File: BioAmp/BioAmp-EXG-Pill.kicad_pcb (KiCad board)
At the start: 2 copper layers, 39.2 x 11 mm, 21 parts, among them IC1 MCP3221A4T-E_OT, J1 Conn_01x03_Pin, J2 Conn_01x04_Pin, J3 Conn_01x04_Pin, U1 Amp

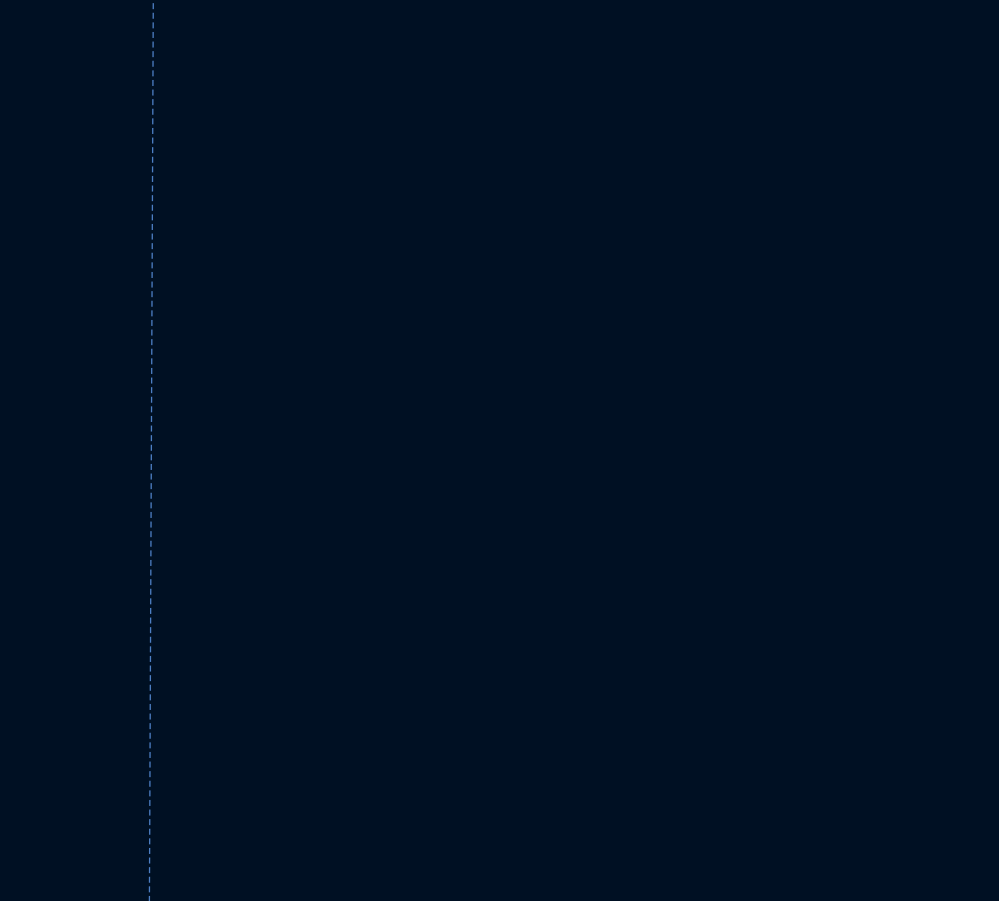
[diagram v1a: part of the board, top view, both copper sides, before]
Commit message: Added new ADC and cleaned up ESD protection
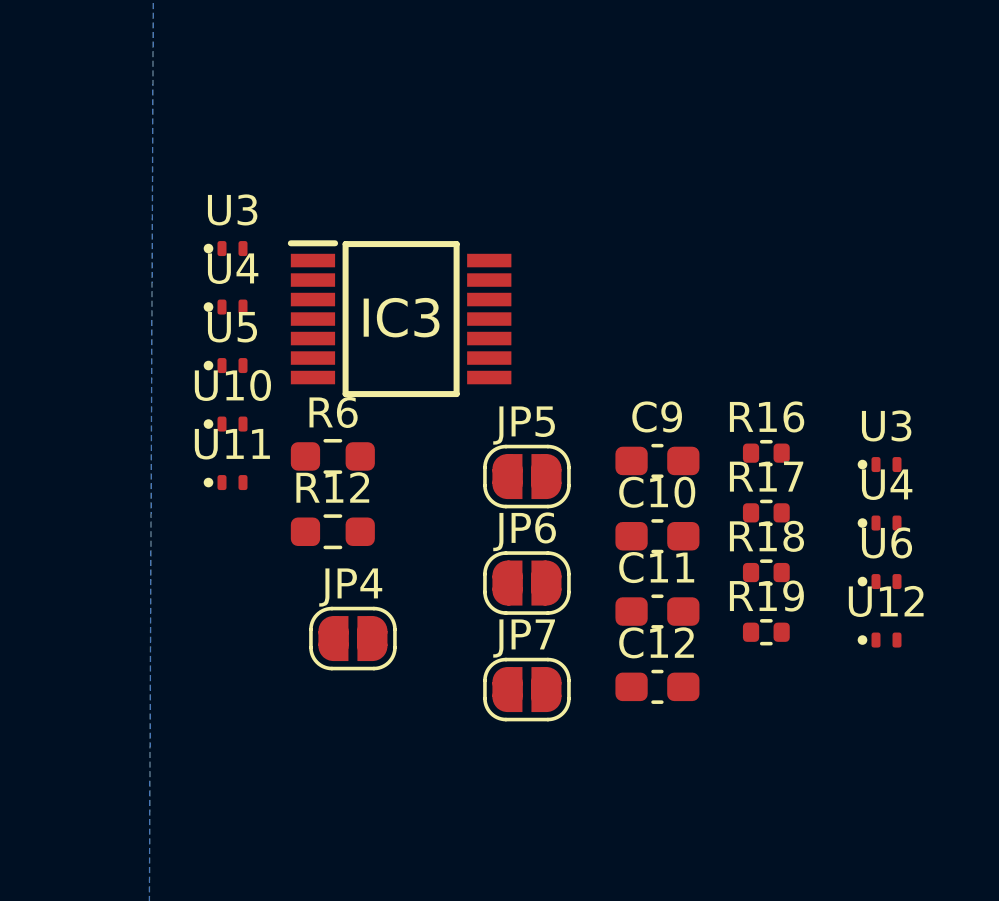
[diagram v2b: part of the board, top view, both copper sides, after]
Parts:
- added C10: 100n, Capacitor_SMD:C_0603_1608Metric_Pad1.08x0.95mm_HandSolder, F.Cu at (176.8, 99.1)
- added C11: 100n, Capacitor_SMD:C_0603_1608Metric_Pad1.08x0.95mm_HandSolder, F.Cu at (176.8, 101.6)
- added C12: 100n, Capacitor_SMD:C_0603_1608Metric_Pad1.08x0.95mm_HandSolder, F.Cu at (176.8, 104.1)
- added C9: 100n, Capacitor_SMD:C_0603_1608Metric_Pad1.08x0.95mm_HandSolder, F.Cu at (176.8, 96.6)
- added IC3: MAX1169BEUD+, MAX1169:SOP65P640X110-14N, F.Cu at (168.3, 91.8)
- added JP4: SolderJumper_2_Open, Jumper:SolderJumper-2_P1.3mm_Open_RoundedPad1.0x1.5mm, F.Cu at (166.7, 102.5)
- added JP5: SolderJumper_2_Open, Jumper:SolderJumper-2_P1.3mm_Open_RoundedPad1.0x1.5mm, F.Cu at (172.5, 97.1)
- added JP6: SolderJumper_2_Open, Jumper:SolderJumper-2_P1.3mm_Open_RoundedPad1.0x1.5mm, F.Cu at (172.5, 100.6)
- added JP7: SolderJumper_2_Open, Jumper:SolderJumper-2_P1.3mm_Open_RoundedPad1.0x1.5mm, F.Cu at (172.5, 104.2)
- added R12: 2.2K, Resistor_SMD:R_0603_1608Metric_Pad0.98x0.95mm_HandSolder, F.Cu at (166.0, 98.9)
- added R16: 10k, Resistor_SMD:R_0402_1005Metric, F.Cu at (180.5, 96.3)
- added R17: 10k, Resistor_SMD:R_0402_1005Metric, F.Cu at (180.5, 98.3)
- added R18: 10k, Resistor_SMD:R_0402_1005Metric, F.Cu at (180.5, 100.3)
- added R19: 10k, Resistor_SMD:R_0402_1005Metric, F.Cu at (180.5, 102.3)
- added R6: 2.2K, Resistor_SMD:R_0603_1608Metric_Pad0.98x0.95mm_HandSolder, F.Cu at (166.0, 96.4)
- added U10: TPD1E05U06DPY, Package_SON:Texas_DPY0002A_0.6x1mm_P0.65mm, F.Cu at (162.7, 95.3)
- added U11: TPD1E05U06DPY, Package_SON:Texas_DPY0002A_0.6x1mm_P0.65mm, F.Cu at (162.7, 97.3)
- added U12: TPD1E05U06DPY, Package_SON:Texas_DPY0002A_0.6x1mm_P0.65mm, F.Cu at (184.5, 102.5)
- added U3: TPD1E05U06DPY, Package_SON:Texas_DPY0002A_0.6x1mm_P0.65mm, F.Cu at (162.7, 89.5)
- added U3: TPD1E05U06DPY, Package_SON:Texas_DPY0002A_0.6x1mm_P0.65mm, F.Cu at (184.5, 96.7)
- added U4: TPD1E05U06DPY, Package_SON:Texas_DPY0002A_0.6x1mm_P0.65mm, F.Cu at (184.5, 98.6)
- added U4: TPD1E05U06DPY, Package_SON:Texas_DPY0002A_0.6x1mm_P0.65mm, F.Cu at (162.7, 91.4)
- added U5: TPD1E05U06DPY, Package_SON:Texas_DPY0002A_0.6x1mm_P0.65mm, F.Cu at (162.7, 93.4)
- added U6: TPD1E05U06DPY, Package_SON:Texas_DPY0002A_0.6x1mm_P0.65mm, F.Cu at (184.5, 100.6)
- C1: value 47uF -> 8.2uF
- C2: value 1nF -> 4.3nF
- C4: value 1nF -> 10pF
- R11: value 0R -> 1M
- R3: value 1M -> 100k
- R4: value 220K -> 270k
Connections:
- IC1 pad 4: SDA -> Net-(IC1-SDA)
- U1 pad 3: IN- -> Net-(U1A-+)
- U1 pad 5: IN+ -> Net-(U1B-+)

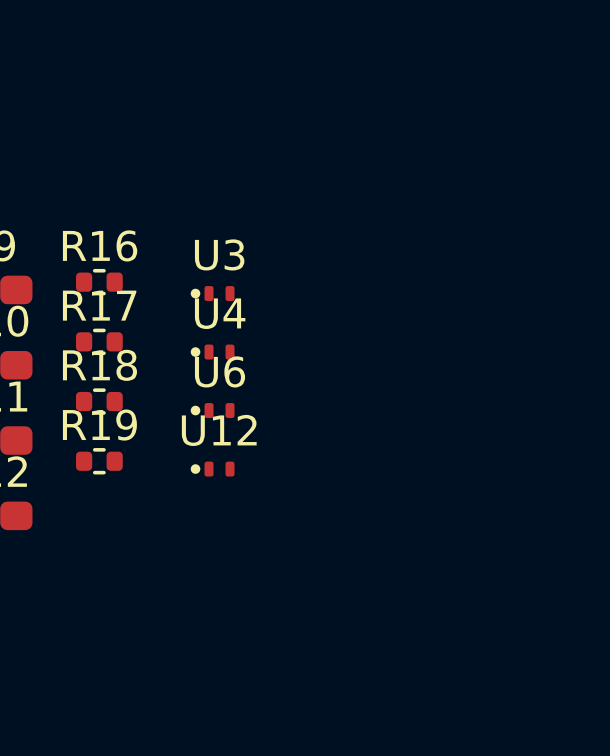
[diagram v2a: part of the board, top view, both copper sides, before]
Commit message: Added series resitors on all electrode connection pins for current limiting
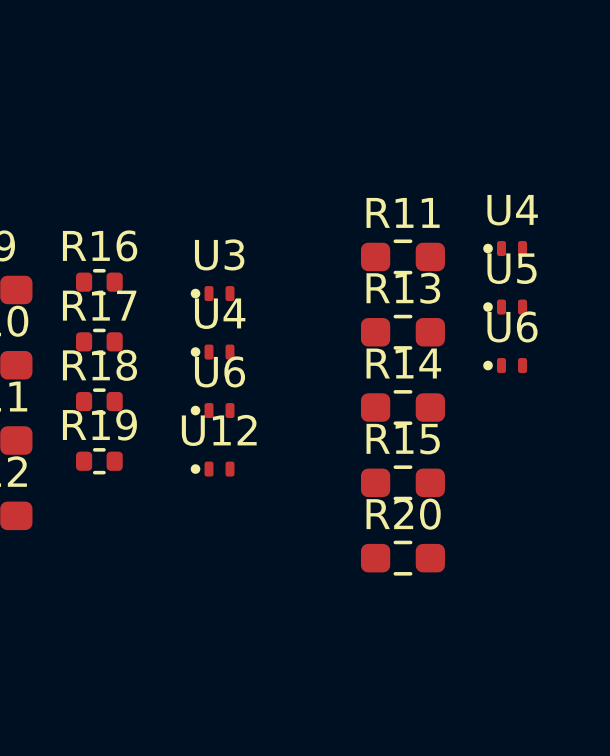
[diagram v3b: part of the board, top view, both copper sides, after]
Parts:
- added R11: 470k, Resistor_SMD:R_0603_1608Metric_Pad0.98x0.95mm_HandSolder, F.Cu at (190.6, 95.5)
- added R13: 470k, Resistor_SMD:R_0603_1608Metric_Pad0.98x0.95mm_HandSolder, F.Cu at (190.6, 98.0)
- added R14: 470k, Resistor_SMD:R_0603_1608Metric_Pad0.98x0.95mm_HandSolder, F.Cu at (190.6, 100.5)
- added R15: 470k, Resistor_SMD:R_0603_1608Metric_Pad0.98x0.95mm_HandSolder, F.Cu at (190.6, 103.0)
- added R20: 470k, Resistor_SMD:R_0603_1608Metric_Pad0.98x0.95mm_HandSolder, F.Cu at (190.6, 105.5)
- added U4: TPD1E05U06DPY, Package_SON:Texas_DPY0002A_0.6x1mm_P0.65mm, F.Cu at (194.2, 95.2)
- added U5: TPD1E05U06DPY, Package_SON:Texas_DPY0002A_0.6x1mm_P0.65mm, F.Cu at (194.2, 97.1)
- added U6: TPD1E05U06DPY, Package_SON:Texas_DPY0002A_0.6x1mm_P0.65mm, F.Cu at (194.2, 99.1)
- R6: value 2.2K -> 470k
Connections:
- R6 pad 1: Net-(U1A-+) -> Net-(R13-Pad2)
- U3 pad 1: unconnected-(U3-I/O-Pad1) -> DRL
- U4 pad 1: unconnected-(U4-I/O-Pad1) -> IN+
- U6 pad 1: unconnected-(U6-I/O-Pad1) -> IN-

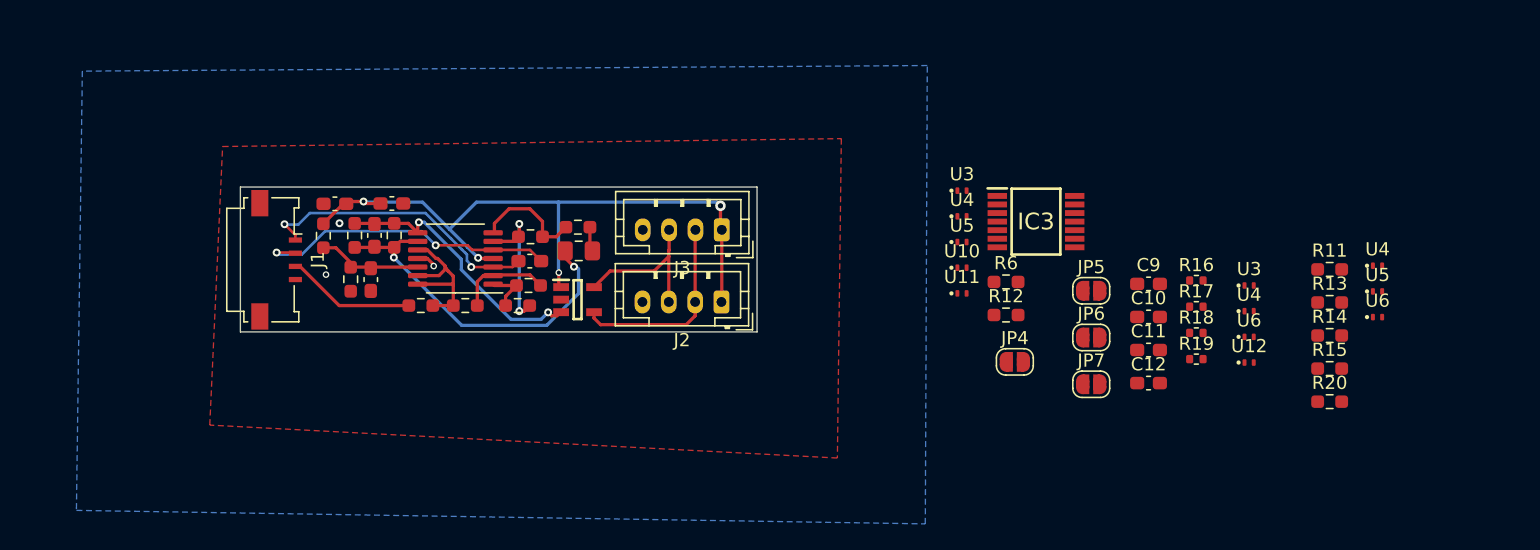
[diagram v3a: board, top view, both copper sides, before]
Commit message: Changed TVS diodes to have lower clamping voltage and added series resitors after protected nodes on opamp
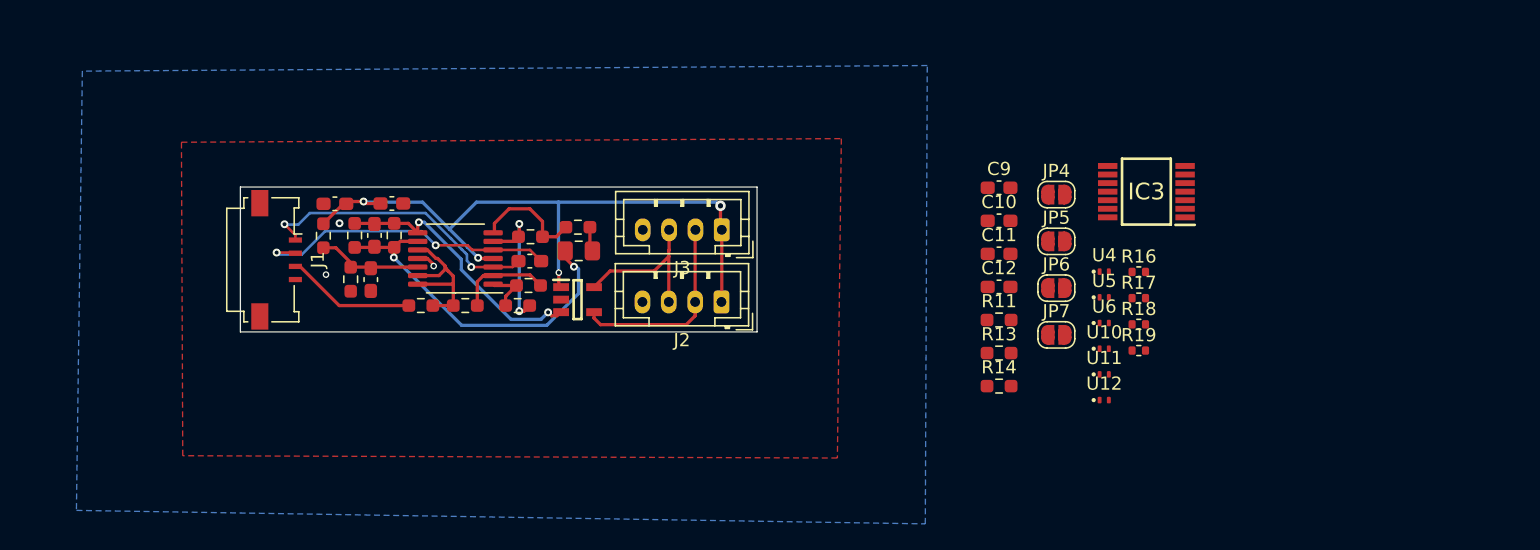
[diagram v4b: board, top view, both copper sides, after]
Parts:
- removed R12: 2.2K, Resistor_SMD:R_0603_1608Metric_Pad0.98x0.95mm_HandSolder
- removed R15, R20, R6: 470k, Resistor_SMD:R_0603_1608Metric_Pad0.98x0.95mm_HandSolder
- removed U3 (x2): TPD1E05U06DPY, Package_SON:Texas_DPY0002A_0.6x1mm_P0.65mm
- removed the U4 at (194.2, 95.2)
- removed the U4 at (184.5, 98.6)
- removed the U4 at (162.7, 91.4)
- removed the U5 at (194.2, 97.1)
- removed the U5 at (162.7, 93.4)
- removed the U6 at (184.5, 100.6)
- removed the U6 at (194.2, 99.1)
- added U4: TPD1E05U06DPY, Package_SON:Texas_DPY0002A_0.6x1mm_P0.65mm, F.Cu at (173.5, 95.6)
- added U5: TPD1E05U06DPY, Package_SON:Texas_DPY0002A_0.6x1mm_P0.65mm, F.Cu at (173.5, 97.6)
- added U6: TPD1E05U06DPY, Package_SON:Texas_DPY0002A_0.6x1mm_P0.65mm, F.Cu at (173.5, 99.5)
- R11, R13, R14: value 470k -> 1M
- moved R11 25.4 mm to (165.5, 99.3)
- moved R13 25.4 mm to (165.5, 101.8)
- moved R14 25.4 mm to (165.5, 104.3)
- moved C9 13.5 mm to (165.5, 89.3)
- moved C10 13.5 mm to (165.5, 91.8)
- moved C11 13.5 mm to (165.5, 94.3)
- moved C12 13.5 mm to (165.5, 96.8)
- moved JP4 13.1 mm to (169.8, 89.8)
- moved U10 12.4 mm to (173.5, 101.5)
- moved U11 12.4 mm to (173.5, 103.4)
- moved U12 11.4 mm to (173.5, 105.4)
- moved IC3 8.69 mm to (176.7, 89.5), turned to 180 degrees
- moved JP5 4.59 mm to (169.8, 93.3)
- moved JP6 4.59 mm to (169.8, 96.9)
- moved JP7 4.59 mm to (169.8, 100.4)
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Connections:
- R11 pad 1: Net-(R11-Pad1) -> DRL
- R13 pad 2: Net-(R13-Pad2) -> IN-
- R14 pad 2: Net-(R14-Pad2) -> IN+

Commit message: Added ESD diode footprints
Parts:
- added D1: ESD441DPLR, Diode_SMD:D_0201_0603Metric, F.Cu at (184.9, 88.5)
- added D2: ESD441DPLR, Diode_SMD:D_0201_0603Metric, F.Cu at (184.9, 90.3)
- added D3: ESD441DPLR, Diode_SMD:D_0201_0603Metric, F.Cu at (184.9, 92.0)
- added D4: ESD441DPLR, Diode_SMD:D_0201_0603Metric, F.Cu at (184.9, 93.8)
- added D5: ESD441DPLR, Diode_SMD:D_0201_0603Metric, F.Cu at (184.9, 95.5)
- added D6: ESD441DPLR, Diode_SMD:D_0201_0603Metric, F.Cu at (184.9, 97.3)
- added R12: 22K, Resistor_SMD:R_0603_1608Metric_Pad0.98x0.95mm_HandSolder, F.Cu at (185.6, 101.9)
- added R15: 22K, Resistor_SMD:R_0603_1608Metric_Pad0.98x0.95mm_HandSolder, F.Cu at (185.6, 104.4)
- added R6: 22K, Resistor_SMD:R_0603_1608Metric_Pad0.98x0.95mm_HandSolder, F.Cu at (185.6, 99.4)
- C12: value 100n -> 10u
- R13, R14: value 1M -> 500k
- U1: value Amp -> TL074HIPWR
- moved IC3 0.16 mm to (176.6, 89.4)
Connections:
- C4 pad 1: IN+ -> /IN+_Prot
- C4 pad 2: IN- -> /IN-_Prot
- R11 pad 2: ampRef -> Net-(D3-K)
- R13 pad 1: Net-(U1A-+) -> Net-(D1-K)
- R14 pad 1: Net-(U1B-+) -> Net-(D2-K)
- U1 pad 3: Net-(U1A-+) -> /IN-_Prot
- U1 pad 5: Net-(U1B-+) -> /IN+_Prot

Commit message: Added models and footprints
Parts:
- added J1: Conn_01x04_Pin, Connector_FFC-FPC:Molex_200528-0040_1x04-1MP_P1.00mm_Horizontal, F.Cu at (196.1, 85.8)
- added J2: Conn_01x04_Pin, Connector_JST:JST_PH_B4B-PH-K_1x04_P2.00mm_Vertical, F.Cu at (192.8, 93.8)
- added J3: Conn_01x04_Pin, Connector_JST:JST_PH_B4B-PH-K_1x04_P2.00mm_Vertical, F.Cu at (192.8, 100.3)

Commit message: Updated FPC connector symbol and footprint
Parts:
- removed the J1 at (196.1, 85.8)
- added J4: 522710469, fpc_con:CON_522710469_MOL, F.Cu at (193.4, 82.7)

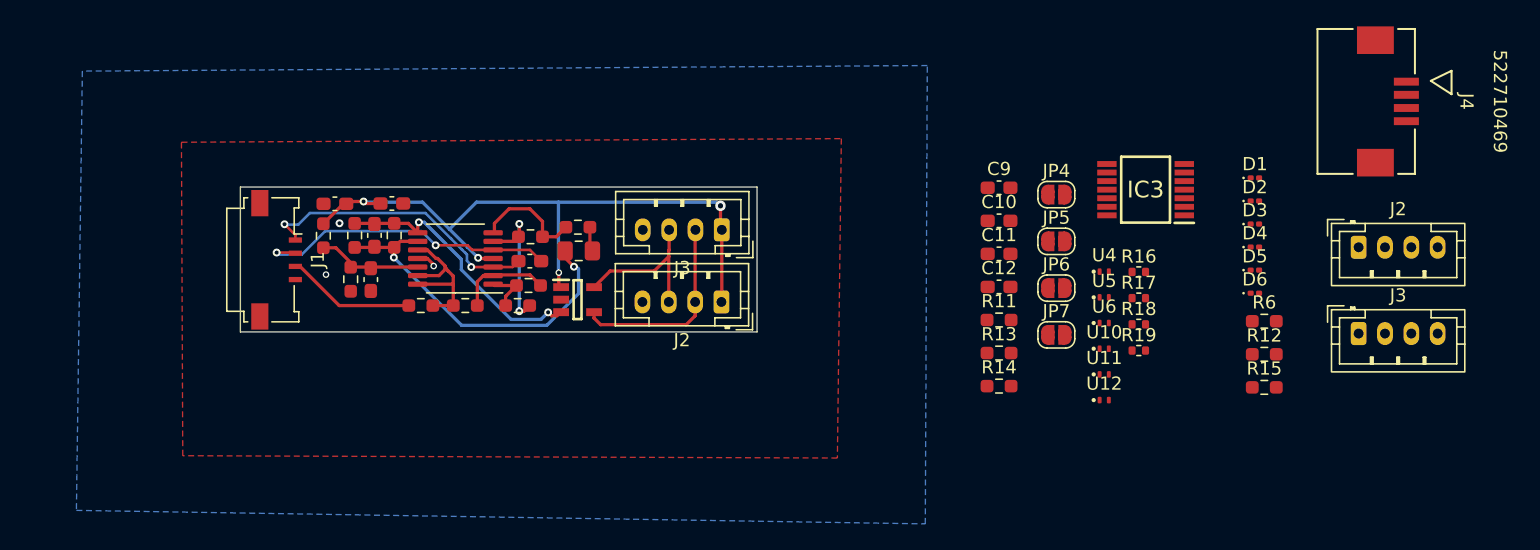
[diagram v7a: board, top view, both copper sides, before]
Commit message: Added board constraints
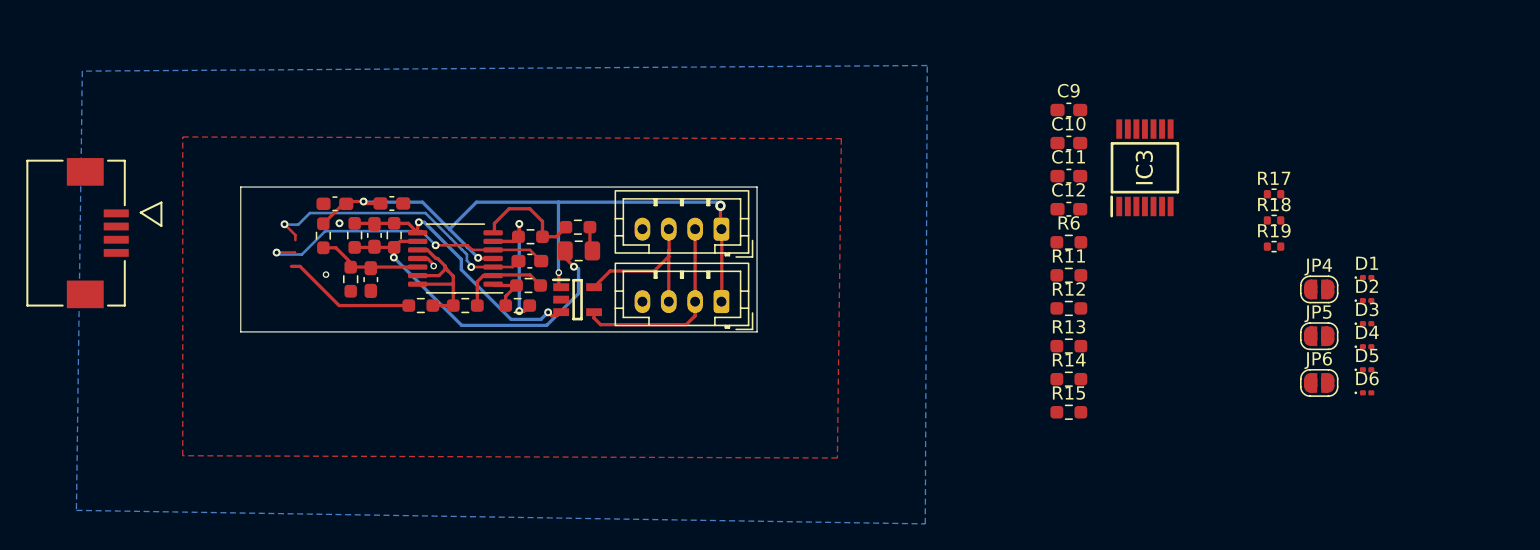
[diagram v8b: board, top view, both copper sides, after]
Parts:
- removed J1: Conn_01x03_Pin, Connector_FFC-FPC:Molex_200528-0040_1x04-1MP_P1.00mm_Horizontal
- removed the J2 at (192.8, 93.8)
- removed the J2 at (144.4, 97.9)
- removed the J3 at (192.8, 100.3)
- removed the J3 at (144.4, 92.5)
- removed JP7: SolderJumper_2_Open, Jumper:SolderJumper-2_P1.3mm_Open_RoundedPad1.0x1.5mm
- removed R16: 10k, Resistor_SMD:R_0402_1005Metric
- removed U10, U11, U12, U4, U5, U6: TPD1E05U06DPY, Package_SON:Texas_DPY0002A_0.6x1mm_P0.65mm
- added J2: Conn_01x04_Pin, Connector_JST:JST_PH_B4B-PH-K_1x04_P2.00mm_Vertical, F.Cu at (144.4, 97.9)
- added J3: Conn_01x04_Pin, Connector_JST:JST_PH_B4B-PH-K_1x04_P2.00mm_Vertical, F.Cu at (144.4, 92.4)
- moved J4 98.5 mm to (95.4, 92.7)
- moved JP5 21.2 mm to (189.8, 100.5)
- moved JP6 21.2 mm to (189.8, 104.1)
- moved JP4 21.2 mm to (189.8, 97.0)
- moved R6 16.0 mm to (170.8, 93.4)
- moved R12 15.2 mm to (170.8, 98.4)
- moved R15 15.0 mm to (170.8, 106.3)
- moved R17 13.0 mm to (186.4, 89.7)
- moved R18 13.0 mm to (186.4, 91.7)
- moved R19 13.0 mm to (186.4, 93.7)
- moved D1 11.4 mm to (193.4, 96.1)
- moved D2 11.4 mm to (193.4, 97.8)
- moved D3 11.4 mm to (193.4, 99.6)
- moved D4 11.4 mm to (193.4, 101.3)
- moved D5 11.4 mm to (193.4, 103.1)
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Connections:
- IC3 pad 14: /ADD3 -> GND
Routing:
- net IN+: track 23.4 -> 0.00 mm, vias 2 -> 1
- net /IN+_Prot: track 0.00 -> 23.4 mm, vias 0 -> 1
- net IN-: track 21.8 -> 0.00 mm, vias 2 -> 1
- net /IN-_Prot: track 0.00 -> 21.8 mm, vias 0 -> 1
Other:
- copper layers 2 -> 4
